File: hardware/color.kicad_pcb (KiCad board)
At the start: 2 copper layers, 25 x 20 mm, 15 parts, among them P1 CON-SENSOR, Q1 2N7002P, U1 TCS3472, U2 M24C64, U3 DRILL, U4 DRILL, U5 DRILL, U6 DRILL

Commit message: add missing logo
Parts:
- added G***: Logo_31x31, Logo_31x31, F.Cu at (104.1, 76.0)
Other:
- board text added: "Copyright Tinkerforge GmbH 2014. This documentation describes Open Hardware and is licensed under the CERN OHL v. 1.1. You may redistribute and modify this documentation under the terms of the CERN OHL v.1.1. (http://ohwr.org/cernohl). This documentation is distributed WITHOUT ANY EXPRESS OR IMPLIED WARRANTY, INCLUDING OF MERCHANTABILITY, SATISFACTORY QUALITY AND FITNESS FOR A PARTICULAR PURPOSE.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"

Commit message: add pull up resistors
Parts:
- added R3: 2k2, 0603, F.Cu at (99.0, 67.9)
- added R4: 2k2, 0603, F.Cu at (100.3, 67.9)
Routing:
- net N-000009: track 5.09 -> 14.5 mm
- net VCC: track 36.1 -> 43.1 mm, vias 4 -> 5
- net N-000008: track 9.69 -> 16.1 mm
- net GND: track 89.6 -> 93.9 mm, vias 11 -> 10

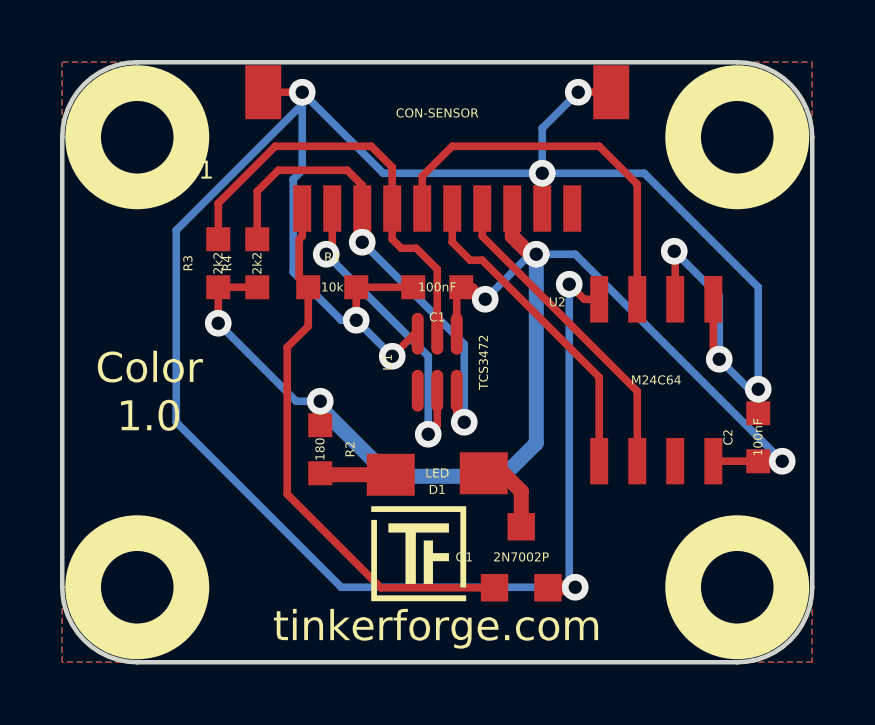
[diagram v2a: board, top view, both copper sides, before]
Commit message: add missing fiducials
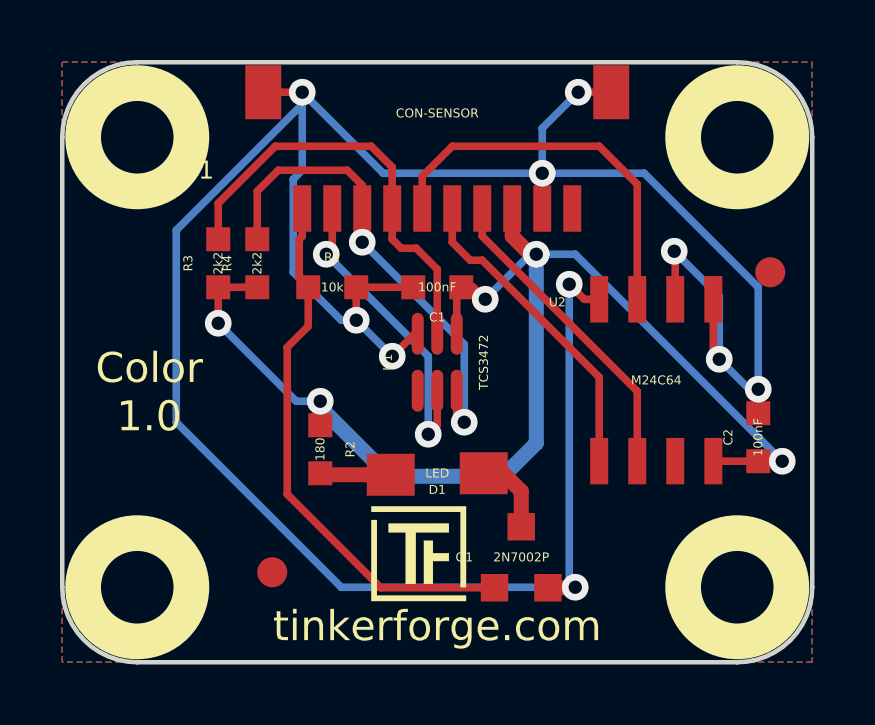
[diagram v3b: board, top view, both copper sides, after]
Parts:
- added Fiducial_Mark: VAL**, Fiducial_Mark, F.Cu at (100.8, 78.2)
- added Fiducial_Mark: VAL**, Fiducial_Mark, F.Cu at (117.4, 68.2)
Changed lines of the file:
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@@
     (links 29)
     (no_connects 0)
-    (area 93.724999 61.124999 118.875001 81.275001)
+    (area 92.844999 60.244999 400.94286 256.6)
     (thickness 1.6)
     (drawings 11)
     (tracks 144)
     (zones 0)
-    (modules 18)
+    (modules 20)
     (nets 12)
   )
@@
     )
   )
+  (module Fiducial_Mark (layer F.Cu)
+    (at 100.8 78.2)
+    (path Fiducial_Mark)
+    (attr smd)
+    (fp_text reference Fiducial_Mark (at 0 0) (layer F.SilkS) hide
+      (effects (font (size 0.127 0.127) (thickness 0.03302)))
+    )
+    (fp_text value VAL** (at 0 -0.29972) (layer F.SilkS) hide
+      (effects (font (size 0.127 0.127) (thickness 0.03302)))
+    )
+    (fp_circle (center 0 0) (end 1.15062 0) (layer Dwgs.User) (width 0.01016))
+    (pad 1 smd circle (at 0 0) (size 1.00076 1.00076)
+      (layers F.Cu F.Mask)
+      (clearance 0.65024)
+    )
+  )
+  (module Fiducial_Mark (layer F.Cu)
+    (at 117.4 68.2)
+    (path Fiducial_Mark)
+    (attr smd)
+    (fp_text reference Fiducial_Mark (at 0 0) (layer F.SilkS) hide
+      (effects (font (size 0.127 0.127) (thickness 0.03302)))
+    )
+    (fp_text value VAL** (at 0 -0.29972) (layer F.SilkS) hide
+      (effects (font (size 0.127 0.127) (thickness 0.03302)))
+    )
+    (fp_circle (center 0 0) (end 1.15062 0) (layer Dwgs.User) (width 0.01016))
+    (pad 1 smd circle (at 0 0) (size 1.00076 1.00076)
+      (layers F.Cu F.Mask)
+      (clearance 0.65024)
+    )
+  )
